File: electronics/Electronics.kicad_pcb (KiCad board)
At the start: 4 copper layers, 102.4 x 75 mm, 85 parts, among them J1 3mm_pad, J10 215079-4, J11 215079-4, J12 215079-4, J13 3mm_pad, J14 3mm_pad, J15 FTSH-105-XX-X-DV, J16 10118193-0001LF, J2 3mm_pad, J3 3mm_pad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

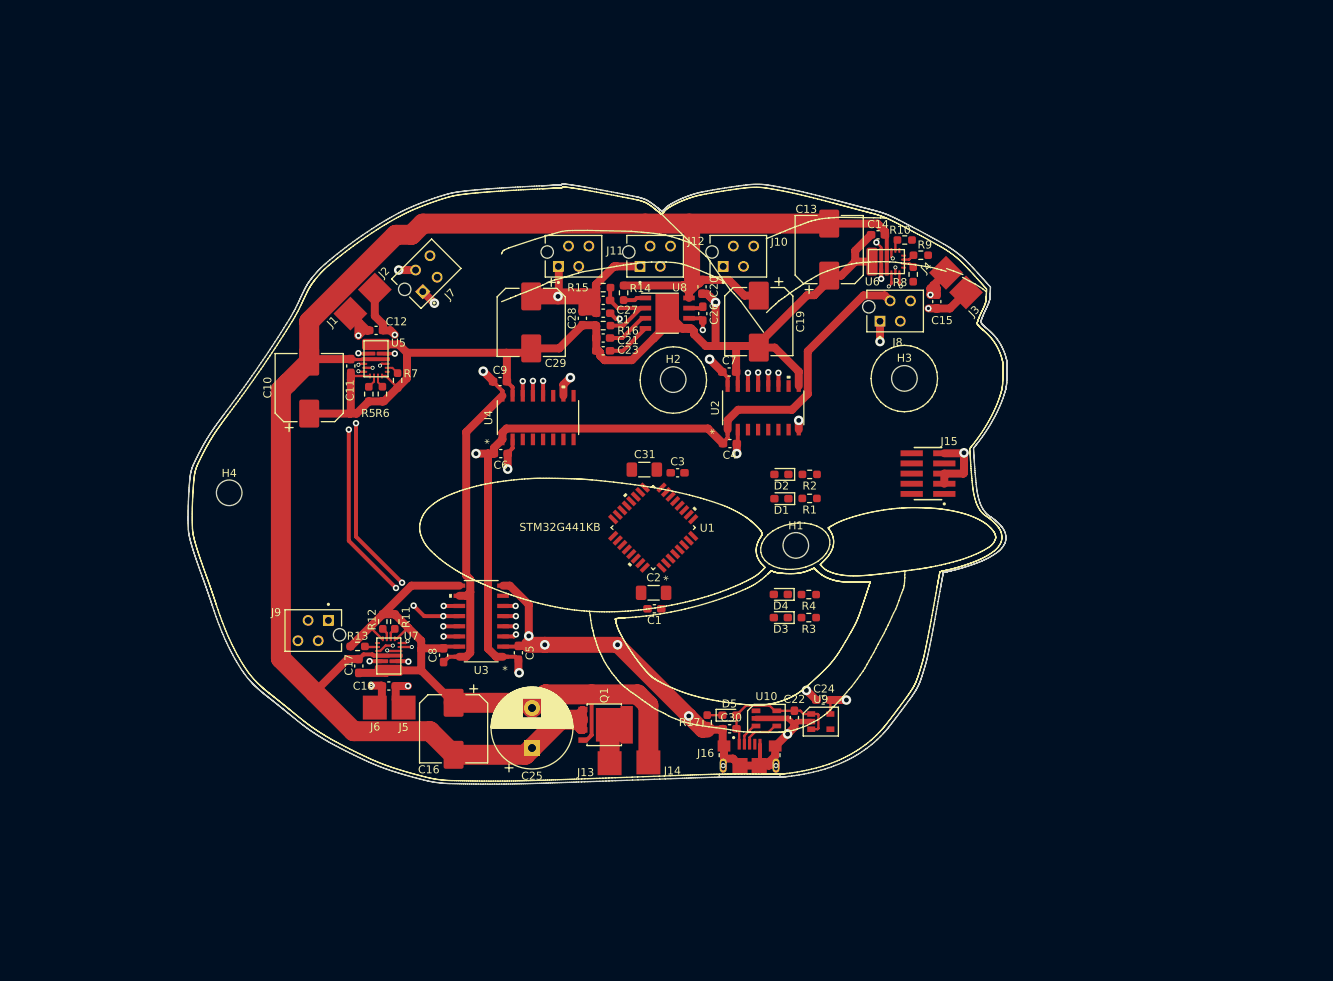
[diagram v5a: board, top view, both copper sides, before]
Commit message: Added MCU to main pcb
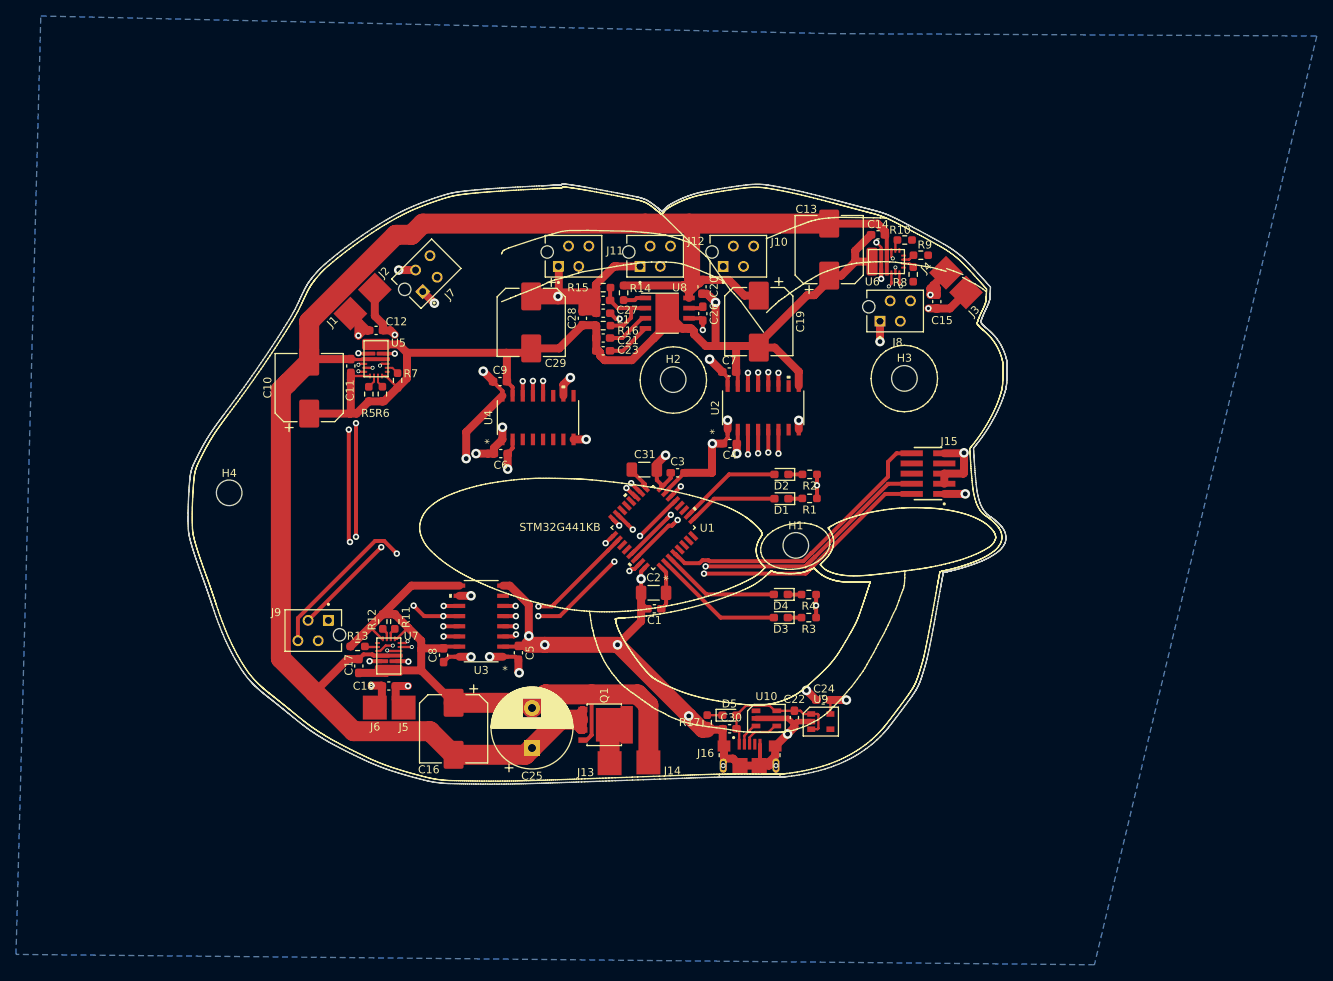
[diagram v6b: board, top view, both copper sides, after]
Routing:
- net +3V3: track 204.2 -> 266.9 mm, vias 4 -> 9
- net /MCU-mot3-enc_2: track 0.00 -> 51.6 mm, vias 0 -> 2
- net /MCU_SWCLK: track 0.00 -> 46.1 mm, vias 0 -> 2
- net /MCU_SWDIO: track 0.00 -> 44.9 mm, vias 0 -> 2
- net /MCU-mot3-enc_1: track 0.00 -> 42.5 mm, vias 0 -> 2
- net /MCU_NRST: track 0.00 -> 37.0 mm
- net GND: track 90.9 -> 120.7 mm, vias 12 -> 18
- net /MCU-mot_sleep: track 1.61 -> 27.5 mm, vias 1 -> 4
- net /MCU-mot_off: track 1.58 -> 19.5 mm, vias 1 -> 2
- net /MCU-debug-LED_G1: track 0.00 -> 16.3 mm
- net /MCU-debug-LED_G2: track 0.00 -> 14.8 mm
- net /MCU-debug-LED_R2: track 0.00 -> 12.8 mm
- net /MCU-debug-LED_R1: track 0.00 -> 11.2 mm
- net /MCU-mot2-enc_2: track 0.00 -> 7.22 mm, vias 0 -> 1
- net /MCU-mot2-enc_1: track 0.00 -> 6.97 mm, vias 0 -> 1
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- added copper zone on B.Cu, net GND

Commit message: Benis :DDDDDDDDDDDDDDDDDDDDD
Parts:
- moved J8 0.85 mm to (143.0, 70.3)
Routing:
- net /MCU-mot1-enc_2: track 0.00 -> 63.4 mm, vias 0 -> 2
- net /MCU-mot1-enc_1: track 0.00 -> 57.3 mm, vias 0 -> 2
- net /MCU-USB_DM: track 3.02 -> 57.7 mm, vias 0 -> 4
- net /MCU-mot2-enc_2: track 7.22 -> 61.0 mm, vias 1 -> 2
- net /MCU-USB_DP: track 4.84 -> 58.2 mm, vias 0 -> 4
- net /MCU-mot2-enc_1: track 6.97 -> 57.0 mm, vias 1 -> 2
- net /MCU-MOT3en_1: track 1.73 -> 37.0 mm, vias 1 -> 4
- net /MCU-Hold-serv_PWM: track 0.00 -> 30.7 mm, vias 0 -> 2
- net /MCU-TRW_PWM: track 0.00 -> 29.5 mm, vias 0 -> 2
- net /MCU-Aim-serv_PWM: track 0.00 -> 27.7 mm, vias 0 -> 2
- net /MCU-MOT3en_2: track 1.61 -> 28.8 mm, vias 1 -> 2
- net /MCU-MOT2en_1: track 2.86 -> 25.7 mm, vias 1 -> 0
- net /MCU-MOT1en_2: track 4.58 -> 24.9 mm, vias 2 -> 4
- net /MCU-MOT2en_2: track 2.99 -> 23.2 mm, vias 1 -> 2
- net /MCU-MOT1en_1: track 4.69 -> 22.0 mm, vias 2 -> 4
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- added copper zone on F.Cu, net Earth
- added copper zone on In1.Cu, net Earth
- added copper zone on In2.Cu, net Earth
- added copper zone on F.Cu, net GND
- added copper zone on In1.Cu, net GND
- added copper zone on In2.Cu, net GND

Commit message: Removed 2 vias, added thermal vias
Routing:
- net /MCU-MOT2en_1: track 25.7 -> 22.9 mm
- net /MCU-MOT1en_1: vias 4 -> 3
- net GND: vias 17 -> 24
- net Earth: vias 16 -> 20
- net /MCU-MOT1en_2: vias 4 -> 3
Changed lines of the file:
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@@
     (thickness 1.6)
     (drawings 11406)
-    (tracks 1170)
+    (tracks 1179)
     (zones 0)
     (modules 85)
@@
   (layers
     (0 F.Cu signal)
-    (1 In1.Cu signal hide)
+    (1 In1.Cu signal)
     (2 In2.Cu signal hide)
     (31 B.Cu signal hide)
@@
   (segment (start 132.845 83.004752) (end 132.845 81.845) (width 1) (layer F.Cu) (net 2))
   (segment (start 125.1 84.75) (end 125.1 86) (width 1) (layer F.Cu) (net 2))
-  (segment (start 132.845 81.845) (end 132.845 81.845) (width 1) (layer F.Cu) (net 2))
   (via (at 132.845 81.845) (size 1.2) (drill 0.6) (layers F.Cu B.Cu) (net 2))
   (segment (start 125.1 86) (end 125.1 86) (width 1) (layer F.Cu) (net 2))
@@
   (segment (start 113.1375 101.6625) (end 113.1375 102.1375) (width 0.5) (layer F.Cu) (net 2))
   (via (at 113.1375 101.6625) (size 1.2) (drill 0.6) (layers F.Cu B.Cu) (net 2))
+  (segment (start 132.845 81.845) (end 132.845 81.845) (width 1) (layer F.Cu) (net 2))
+  (via (at 147.7 96.2) (size 1.2) (drill 0.6) (layers F.Cu B.Cu) (net 2))
+  (via (at 140.6 96.6) (size 1.2) (drill 0.6) (layers F.Cu B.Cu) (net 2))
+  (via (at 140.8 109) (size 1.2) (drill 0.6) (layers F.Cu B.Cu) (net 2))
+  (via (at 118.9 111.5) (size 1.2) (drill 0.6) (layers F.Cu B.Cu) (net 2))
+  (via (at 123.3 102.6) (size 1.2) (drill 0.6) (layers F.Cu B.Cu) (net 2))
+  (via (at 96.7 94.2) (size 1.2) (drill 0.6) (layers F.Cu B.Cu) (net 2))
+  (via (at 100.2 101.3) (size 1.2) (drill 0.6) (layers F.Cu B.Cu) (net 2))
   (via (at 82.35 73.5) (size 0.8) (drill 0.4) (layers F.Cu B.Cu) (net 3))
   (segment (start 82.35 71.3) (end 82.35 71.3) (width 0.4) (layer In1.Cu) (net 3))
@@
   (via (at 153.6 76.7) (size 1.2) (drill 0.6) (layers F.Cu B.Cu) (net 12))
   (via (at 153.4 71.4) (size 1.2) (drill 0.6) (layers F.Cu B.Cu) (net 12))
-  (via (at 127 54.5) (size 1.2) (drill 0.6) (layers F.Cu B.Cu) (net 12))
+  (via (at 131.7 54.5) (size 1.2) (drill 0.6) (layers F.Cu B.Cu) (net 12))
   (via (at 107.3 54.8) (size 1.2) (drill 0.6) (layers F.Cu B.Cu) (net 12))
   (via (at 93.4 54.8) (size 1.2) (drill 0.6) (layers F.Cu B.Cu) (net 12))
-  (via (at 122 54.8) (size 1.2) (drill 0.6) (layers F.Cu B.Cu) (net 12))
+  (via (at 122.4 54.5) (size 1.2) (drill 0.6) (layers F.Cu B.Cu) (net 12))
   (via (at 140.1 72.7) (size 1.2) (drill 0.6) (layers F.Cu B.Cu) (net 12))
   (via (at 136.4 76.7) (size 1.2) (drill 0.6) (layers F.Cu B.Cu) (net 12))
@@
   (via (at 85.6 93.3) (size 1.2) (drill 0.6) (layers F.Cu B.Cu) (net 12))
   (via (at 61.1 95.5) (size 1.2) (drill 0.6) (layers F.Cu B.Cu) (net 12))
+  (via (at 93.9 62.1) (size 1.2) (drill 0.6) (layers F.Cu B.Cu) (net 12))
+  (via (at 93.7 70.1) (size 1.2) (drill 0.6) (layers F.Cu B.Cu) (net 12))
+  (via (at 111.1 77.3) (size 1.2) (drill 0.6) (layers F.Cu B.Cu) (net 12))
+  (via (at 64 106) (size 1.2) (drill 0.6) (layers F.Cu B.Cu) (net 12))
   (segment (start 107.5375 65.3) (end 107.4875 65.25) (width 1) (layer F.Cu) (net 14))
   (segment (start 107.3 68.225) (end 107.525 68.45) (width 1) (layer F.Cu) (net 14))
@@
   (segment (start 97.485 107.585) (end 97.947001 107.122999) (width 0.5) (layer In1.Cu) (net 33))
   (segment (start 127.765 83.004752) (end 127.765 85.965) (width 0.5) (layer F.Cu) (net 34))
-  (segment (start 127.765 85.965) (end 127.765 85.965) (width 0.5) (layer F.Cu) (net 34))
-  (via (at 127.765 85.965) (size 0.8) (drill 0.4) (layers F.Cu B.Cu) (net 34))
   (segment (start 112.476672 91.379616) (end 112.476672 91.376672) (width 0.5) (layer F.Cu) (net 34))
   (segment (start 112.476672 91.376672) (end 110.8 89.7) (width 0.5) (layer F.Cu) (net 34))
@@
   (segment (start 127.765 86.411586) (end 127.765 85.965) (width 0.5) (layer F.Cu) (net 34))
   (segment (start 125.5 90.4) (end 126.46898 89.43102) (width 0.5) (layer F.Cu) (net 34))
-  (segment (start 126.495 83.004752) (end 126.495 86.095) (width 0.5) (layer F.Cu) (net 35))
-  (segment (start 126.495 86.095) (end 126.495 86.095) (width 0.5) (layer F.Cu) (net 35))
-  (via (at 126.495 86.095) (size 0.8) (drill 0.4) (layers F.Cu B.Cu) (net 35))
+  (segment (start 127.765 85.965) (end 127.765 85.965) (width 0.5) (layer F.Cu) (net 34))
   (segment (start 113.042358 90.81393) (end 113.01393 90.81393) (width 0.5) (layer F.Cu) (net 35))
   (segment (start 113.01393 90.81393) (end 111.9 89.7) (width 0.5) (layer F.Cu) (net 35))
@@
   (segment (start 124.5 90.3) (end 124.5 90.3) (width 0.5) (layer In1.Cu) (net 35))
   (via (at 124.5 90.3) (size 0.8) (drill 0.4) (layers F.Cu B.Cu) (net 35))
-  (segment (start 126.495 86.095) (end 125.827622 86.762378) (width 0.5) (layer F.Cu) (net 35))
   (segment (start 125.827622 88.972378) (end 124.5 90.3) (width 0.5) (layer F.Cu) (net 35))
-  (segment (start 125.827622 86.762378) (end 125.827622 88.972378) (width 0.5) (layer F.Cu) (net 35))
+  (segment (start 125.841971 88.858029) (end 125.841972 87.447888) (width 0.5) (layer F.Cu) (net 35))
+  (segment (start 125.827622 88.872378) (end 125.841971 88.858029) (width 0.5) (layer F.Cu) (net 35))
+  (segment (start 125.827622 88.972378) (end 125.827622 88.872378) (width 0.5) (layer F.Cu) (net 35))
+  (segment (start 125.841972 87.447888) (end 126.495 86.79486) (width 0.5) (layer F.Cu) (net 35))
+  (segment (start 126.495 86.79486) (end 126.495 83.004752) (width 0.5) (layer F.Cu) (net 35))
   (segment (start 95.874752 106.315) (end 97.485 106.315) (width 0.5) (layer F.Cu) (net 36))
   (segment (start 97.485 106.315) (end 97.485 106.315) (width 0.5) (layer F.Cu) (net 36))
@@
   (segment (start 121.2 97.7) (end 121.007844 97.892156) (width 0.5) (layer F.Cu) (net 43))
   (segment (start 121.8 97.7) (end 121.2 97.7) (width 0.5) (layer F.Cu) (net 43))
-  (segment (start 129.035 83.004752) (end 129.035 85.865) (width 0.5) (layer F.Cu) (net 44))
-  (segment (start 129.035 86.028312) (end 129.035 83.004752) (width 0.5) (layer F.Cu) (net 44))
   (segment (start 127.09599 87.967322) (end 129.035 86.028312) (width 0.5) (layer F.Cu) (net 44))
   (segment (start 122.254002 98.545998) (end 127.095989 93.704011) (width 0.5) (layer F.Cu) (net 44))
@@
   (segment (start 127.095989 93.704011) (end 127.09599 87.967322) (width 0.5) (layer F.Cu) (net 44))
   (segment (start 117.954698 97.989014) (end 117.989014 97.989014) (width 0.5) (layer F.Cu) (net 44))
+  (segment (start 129.035 86.028312) (end 129.035 83.004752) (width 0.5) (layer F.Cu) (net 44))
   (segment (start 117.389014 98.554698) (end 118.157315 99.322999) (width 0.5) (layer F.Cu) (net 45))
   (segment (start 144 88.875962) (end 144 88.875962) (width 0.5) (layer In1.Cu) (net 45))
